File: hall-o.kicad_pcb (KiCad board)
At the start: 2 copper layers, 28.4 x 12.4 mm, 16 parts, among them P1 CONN_01X04, Q1 BC848, U1 ss495b, U2 LM258D

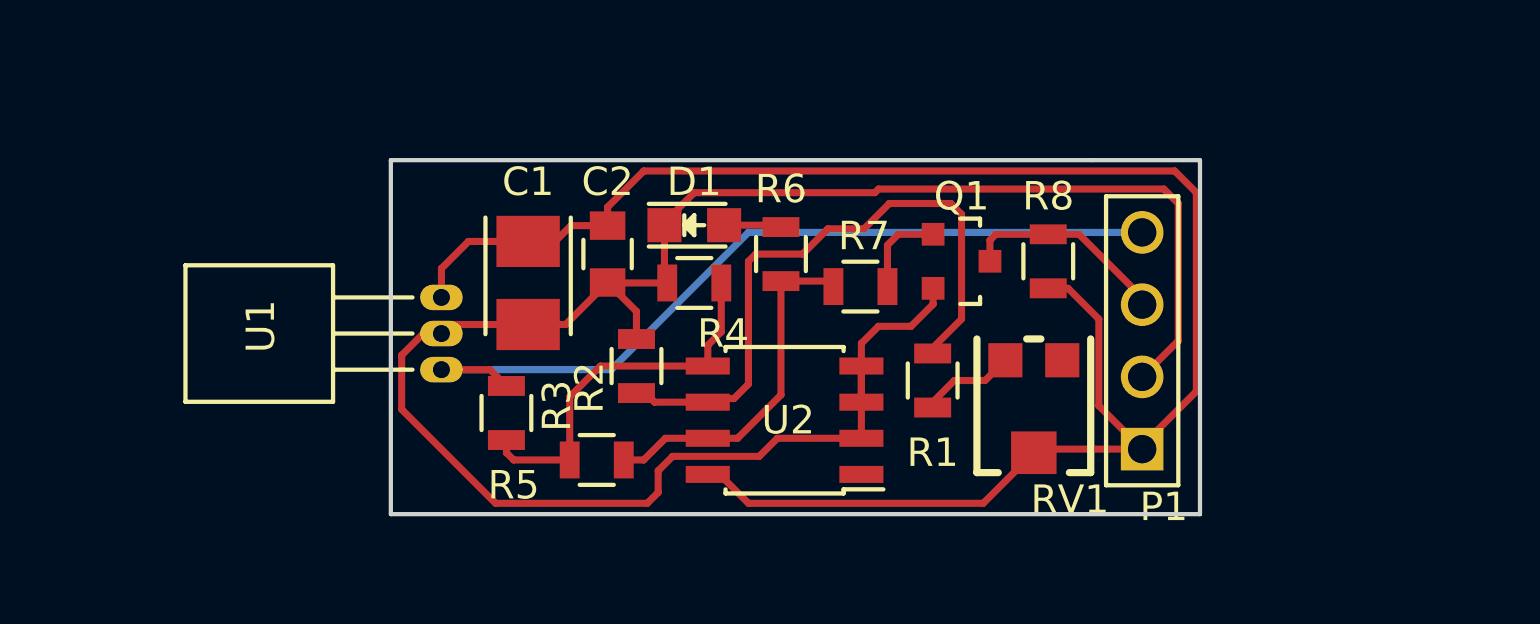
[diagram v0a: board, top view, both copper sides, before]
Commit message: thickened traces
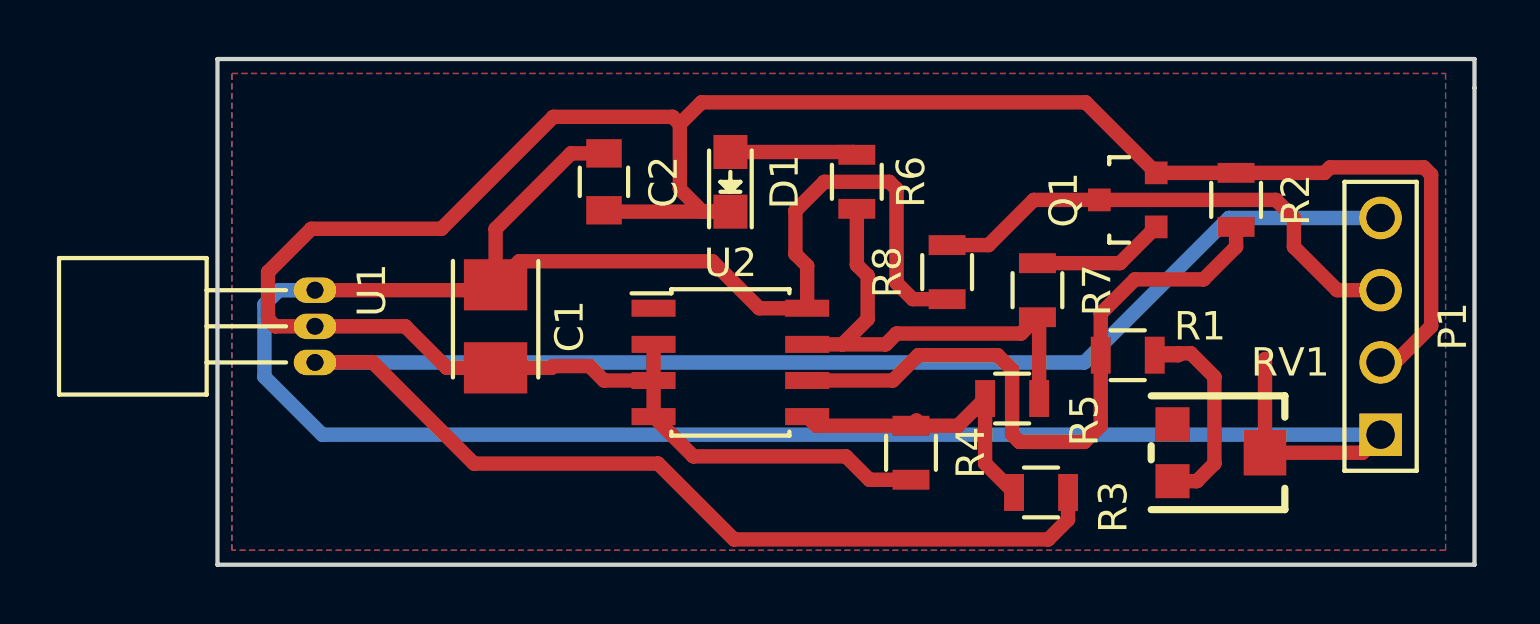
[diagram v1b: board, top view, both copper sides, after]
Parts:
- moved R2 21.9 mm to (153.7, 98.4)
- moved R3 19.0 mm to (146.8, 108.7), turned to 180 degrees
- moved R5 14.8 mm to (145.8, 105.4)
- moved R4 9.68 mm to (142.2, 107.3), turned to 270 degrees
- moved P1 8.40 mm to (158.8, 102.9)
- moved R1 6.92 mm to (149.9, 103.9), turned to 0 degrees
- moved RV1 6.68 mm to (153.0, 107.3), turned to 270 degrees
- moved Q1 6.23 mm to (149.9, 98.4), turned to 90 degrees
- moved R7 6.22 mm to (146.7, 101.6), turned to 270 degrees
- moved U1 4.45 mm to (121.3, 101.6)
- moved R6 3.68 mm to (140.3, 97.8)
- moved R8 3.58 mm to (143.5, 101.0)
- moved U2 2.79 mm to (135.9, 104.1), turned to 0 degrees
- moved C2 2.54 mm to (131.4, 97.8)
- moved D1 1.98 mm to (135.9, 97.8), turned to 90 degrees
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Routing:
- net /SIG: track 29.2 -> 69.9 mm
- net /+5V: track 63.6 -> 90.5 mm
- net /GND: track 70.0 -> 89.9 mm
- net /STOP: track 7.35 -> 17.8 mm
- net Net-(R1-Pad2): track 3.35 -> 7.79 mm
- net Net-(R5-Pad1): track 12.7 -> 16.7 mm
- net Net-(R3-Pad2): track 13.4 -> 10.8 mm
- net Net-(D1-Pad2): track 2.03 -> 4.49 mm
- net Net-(Q1-Pad1): track 3.22 -> 4.70 mm
- net Net-(R1-Pad1): track 22.5 -> 23.9 mm
- added copper zone on B.Cu, net /+5V
- added copper zone on F.Cu, net /GND
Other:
- board size 28.4 x 12.4 mm -> 44.2 x 17.8 mm
